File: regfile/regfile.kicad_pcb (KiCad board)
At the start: 2 copper layers, 5 parts, among them J1 Conn_01x39_Pin, U1 74LS170, U18 74LS170, U2 74LS170, U3 74LS170

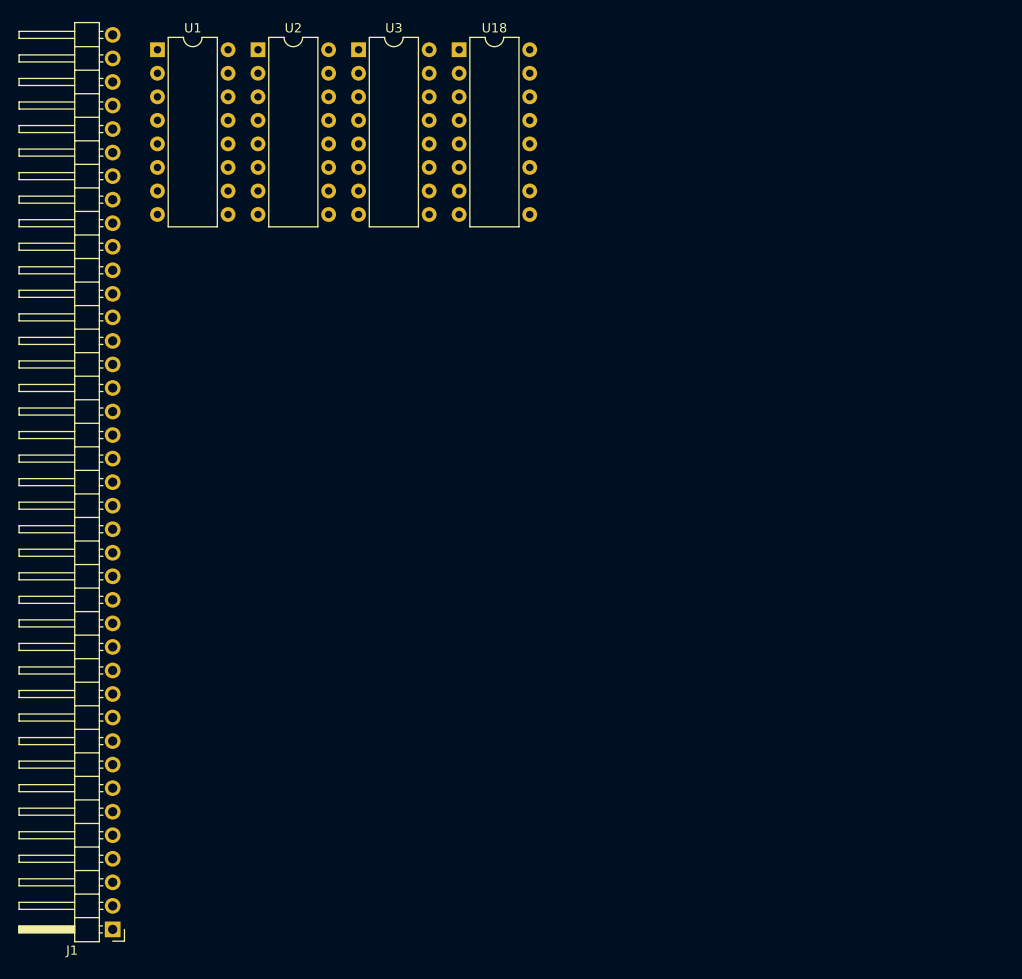
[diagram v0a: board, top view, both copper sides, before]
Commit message: fix logic for the regfile
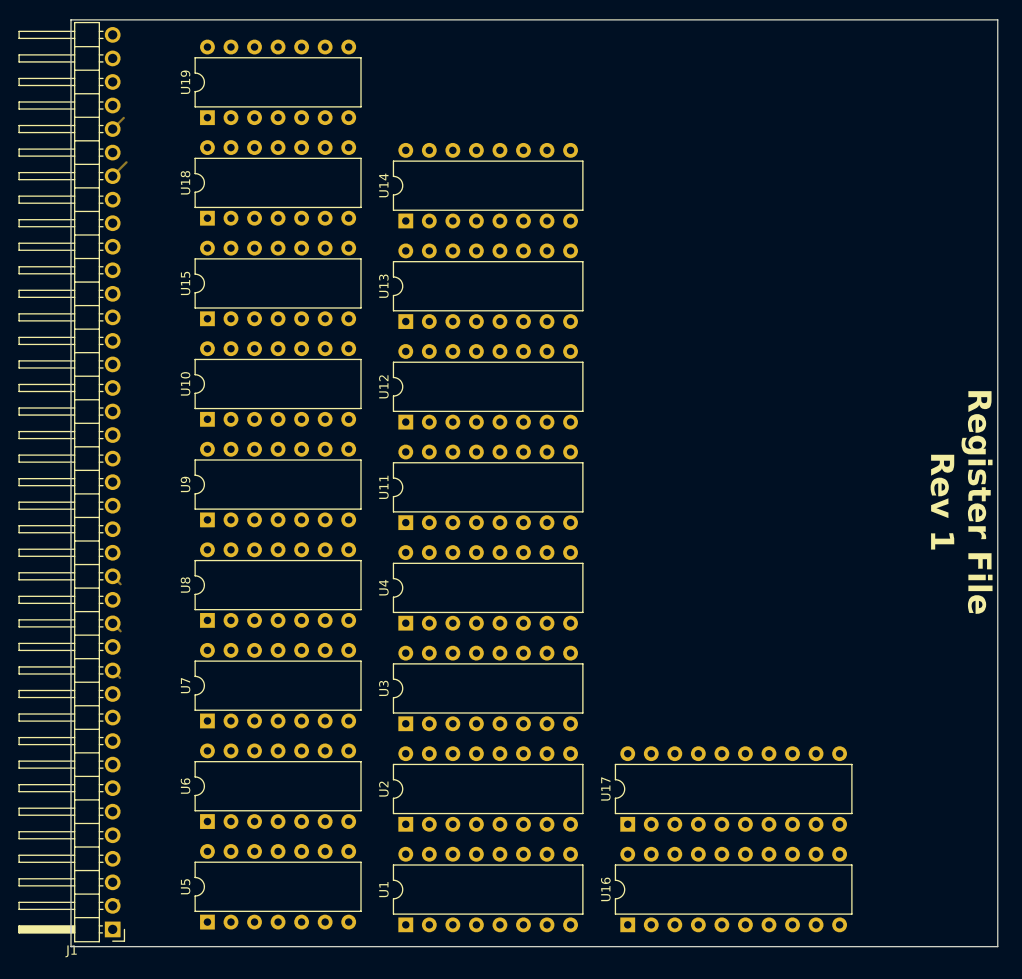
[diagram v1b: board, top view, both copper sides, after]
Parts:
- added U10: 74LS32, Package_DIP:DIP-14_W7.62mm, F.Cu at (108.2, 79.1)
- added U11: 74LS670, Package_DIP:DIP-16_W7.62mm, F.Cu at (129.6, 90.2)
- added U12: 74LS670, Package_DIP:DIP-16_W7.62mm, F.Cu at (129.6, 79.4)
- added U13: 74LS670, Package_DIP:DIP-16_W7.62mm, F.Cu at (129.6, 68.5)
- added U14: 74LS670, Package_DIP:DIP-16_W7.62mm, F.Cu at (129.6, 57.7)
- added U15: 74LS32, Package_DIP:DIP-14_W7.62mm, F.Cu at (108.2, 68.2)
- added U16: 74LS244, Package_DIP:DIP-20_W7.62mm, F.Cu at (153.6, 133.7)
- added U17: 74LS244, Package_DIP:DIP-20_W7.62mm, F.Cu at (153.6, 122.8)
- added U19: 74HC04, Package_DIP:DIP-14_W7.62mm, F.Cu at (108.2, 46.5)
- added U4: 74LS670, Package_DIP:DIP-16_W7.62mm, F.Cu at (129.6, 101.1)
- added U5: 74LS00, Package_DIP:DIP-14_W7.62mm, F.Cu at (108.2, 133.3)
- added U6: 74LS00, Package_DIP:DIP-14_W7.62mm, F.Cu at (108.2, 122.5)
- added U7: 74LS00, Package_DIP:DIP-14_W7.62mm, F.Cu at (108.2, 111.7)
- added U8: 74LS00, Package_DIP:DIP-14_W7.62mm, F.Cu at (108.2, 100.8)
- added U9: 74HC04, Package_DIP:DIP-14_W7.62mm, F.Cu at (108.2, 90.0)
- U1, U2, U3: value 74LS170 -> 74LS670
- U18: value 74LS170 -> 74LS27; footprint Package_DIP:DIP-16_W7.62mm -> Package_DIP:DIP-14_W7.62mm
- moved U1 98.2 mm to (129.6, 133.7), turned to 90 degrees
- moved U2 85.1 mm to (129.6, 122.8), turned to 90 degrees
- moved U3 72.9 mm to (129.6, 112.0), turned to 90 degrees
- moved U18 32.7 mm to (108.2, 57.4), turned to 90 degrees
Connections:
- J1 pad 10: unconnected-(J1-Pin_10-Pad10) -> Net-(J1-Pin_10)
- J1 pad 11: unconnected-(J1-Pin_11-Pad11) -> Net-(J1-Pin_11)
- J1 pad 12: unconnected-(J1-Pin_12-Pad12) -> Net-(J1-Pin_12)
- J1 pad 13: unconnected-(J1-Pin_13-Pad13) -> Net-(J1-Pin_13)
- J1 pad 14: unconnected-(J1-Pin_14-Pad14) -> Net-(J1-Pin_14)
- J1 pad 15: unconnected-(J1-Pin_15-Pad15) -> Net-(J1-Pin_15)
- J1 pad 16: unconnected-(J1-Pin_16-Pad16) -> Net-(J1-Pin_16)
- J1 pad 17: unconnected-(J1-Pin_17-Pad17) -> Net-(J1-Pin_17)
- J1 pad 18: unconnected-(J1-Pin_18-Pad18) -> Net-(J1-Pin_18)
- J1 pad 19: unconnected-(J1-Pin_19-Pad19) -> Net-(J1-Pin_19)
- J1 pad 20: unconnected-(J1-Pin_20-Pad20) -> Net-(J1-Pin_20)
- J1 pad 21: unconnected-(J1-Pin_21-Pad21) -> Net-(J1-Pin_21)
- J1 pad 22: unconnected-(J1-Pin_22-Pad22) -> Net-(J1-Pin_22)
- J1 pad 23: unconnected-(J1-Pin_23-Pad23) -> Net-(J1-Pin_23)
- J1 pad 24: unconnected-(J1-Pin_24-Pad24) -> Net-(J1-Pin_24)
- J1 pad 25: unconnected-(J1-Pin_25-Pad25) -> Net-(J1-Pin_25)
- J1 pad 26: unconnected-(J1-Pin_26-Pad26) -> Net-(J1-Pin_26)
- J1 pad 27: unconnected-(J1-Pin_27-Pad27) -> Net-(J1-Pin_27)
- J1 pad 28: unconnected-(J1-Pin_28-Pad28) -> Net-(J1-Pin_28)
- J1 pad 29: unconnected-(J1-Pin_29-Pad29) -> Net-(J1-Pin_29)
- J1 pad 30: unconnected-(J1-Pin_30-Pad30) -> Net-(J1-Pin_30)
- J1 pad 31: unconnected-(J1-Pin_31-Pad31) -> Net-(J1-Pin_31)
- J1 pad 32: unconnected-(J1-Pin_32-Pad32) -> Net-(J1-Pin_32)
- J1 pad 33: unconnected-(J1-Pin_33-Pad33) -> Net-(J1-Pin_33)
- J1 pad 34: unconnected-(J1-Pin_34-Pad34) -> Net-(J1-Pin_34)
- J1 pad 35: unconnected-(J1-Pin_35-Pad35) -> Net-(J1-Pin_35)
- J1 pad 36: unconnected-(J1-Pin_36-Pad36) -> Net-(J1-Pin_36)
- J1 pad 37: unconnected-(J1-Pin_37-Pad37) -> Net-(J1-Pin_37)
- J1 pad 38: unconnected-(J1-Pin_38-Pad38) -> Net-(J1-Pin_38)
- J1 pad 39: unconnected-(J1-Pin_39-Pad39) -> Net-(J1-Pin_39)
- J1 pad 7: unconnected-(J1-Pin_7-Pad7) -> Net-(J1-Pin_7)
- J1 pad 8: unconnected-(J1-Pin_8-Pad8) -> Net-(J1-Pin_8)
- J1 pad 9: unconnected-(J1-Pin_9-Pad9) -> Net-(J1-Pin_9)
- U1 pad 1: unconnected-(U1-D2-Pad1) -> Net-(J1-Pin_17)
- U1 pad 10: unconnected-(U1-Q1-Pad10) -> Net-(J1-Pin_24)
- U1 pad 11: unconnected-(U1-~{Er}-Pad11) -> Net-(U1-~{Er})
- U1 pad 12: unconnected-(U1-~{Ew}-Pad12) -> Net-(U1-~{Ew})
- U1 pad 13: unconnected-(U1-Wb-Pad13) -> Net-(J1-Pin_8)
- U1 pad 14: unconnected-(U1-Wa-Pad14) -> Net-(J1-Pin_7)
- U1 pad 15: unconnected-(U1-D1-Pad15) -> Net-(J1-Pin_16)
- U1 pad 2: unconnected-(U1-D3-Pad2) -> Net-(J1-Pin_18)
- U1 pad 3: unconnected-(U1-D4-Pad3) -> Net-(J1-Pin_19)
- U1 pad 4: unconnected-(U1-Rb-Pad4) -> Net-(J1-Pin_11)
- U1 pad 5: unconnected-(U1-Ra-Pad5) -> Net-(J1-Pin_10)
- U1 pad 6: unconnected-(U1-Q4-Pad6) -> Net-(J1-Pin_27)
- U1 pad 7: unconnected-(U1-Q3-Pad7) -> Net-(J1-Pin_26)
- U1 pad 9: unconnected-(U1-Q2-Pad9) -> Net-(J1-Pin_25)
- U18 pad 1: unconnected-(U18-D2-Pad1) -> Net-(J1-Pin_10)
- U18 pad 10: unconnected-(U18-Q1-Pad10) -> GND
- U18 pad 11: unconnected-(U18-~{Er}-Pad11) -> GND
- U18 pad 12: unconnected-(U18-~{Ew}-Pad12) -> ZR_addr1
- U18 pad 13: unconnected-(U18-Wb-Pad13) -> Net-(J1-Pin_12)
- U18 pad 14: unconnected-(U18-Wa-Pad14) -> +5V
- U18 pad 2: unconnected-(U18-D3-Pad2) -> Net-(J1-Pin_11)
- U18 pad 3: unconnected-(U18-D4-Pad3) -> Net-(J1-Pin_15)
- U18 pad 4: unconnected-(U18-Rb-Pad4) -> Net-(J1-Pin_14)
- U18 pad 5: unconnected-(U18-Ra-Pad5) -> Net-(J1-Pin_13)
- U18 pad 6: unconnected-(U18-Q4-Pad6) -> ZR_addr2
- U18 pad 7: unconnected-(U18-Q3-Pad7) -> GND
- U18 pad 8: GND -> unconnected-(U18-Pad8)
- U18 pad 9: unconnected-(U18-Q2-Pad9) -> GND
- U2 pad 1: unconnected-(U2-D2-Pad1) -> Net-(J1-Pin_21)
- U2 pad 10: unconnected-(U2-Q1-Pad10) -> Net-(J1-Pin_28)
- U2 pad 11: unconnected-(U2-~{Er}-Pad11) -> Net-(U2-~{Er})
- U2 pad 12: unconnected-(U2-~{Ew}-Pad12) -> Net-(U2-~{Ew})
- U2 pad 13: unconnected-(U2-Wb-Pad13) -> Net-(J1-Pin_8)
- U2 pad 14: unconnected-(U2-Wa-Pad14) -> Net-(J1-Pin_7)
- U2 pad 15: unconnected-(U2-D1-Pad15) -> Net-(J1-Pin_20)
- U2 pad 2: unconnected-(U2-D3-Pad2) -> Net-(J1-Pin_22)
- U2 pad 3: unconnected-(U2-D4-Pad3) -> Net-(J1-Pin_23)
- U2 pad 4: unconnected-(U2-Rb-Pad4) -> Net-(J1-Pin_11)
- U2 pad 5: unconnected-(U2-Ra-Pad5) -> Net-(J1-Pin_10)
- U2 pad 6: unconnected-(U2-Q4-Pad6) -> Net-(J1-Pin_31)
- U2 pad 7: unconnected-(U2-Q3-Pad7) -> Net-(J1-Pin_30)
- U2 pad 9: unconnected-(U2-Q2-Pad9) -> Net-(J1-Pin_29)
- U3 pad 1: unconnected-(U3-D2-Pad1) -> Net-(J1-Pin_17)
- U3 pad 10: unconnected-(U3-Q1-Pad10) -> Net-(J1-Pin_24)
- U3 pad 11: unconnected-(U3-~{Er}-Pad11) -> Net-(U3-~{Er})
- U3 pad 12: unconnected-(U3-~{Ew}-Pad12) -> Net-(U3-~{Ew})
- U3 pad 13: unconnected-(U3-Wb-Pad13) -> Net-(J1-Pin_8)
- U3 pad 14: unconnected-(U3-Wa-Pad14) -> Net-(J1-Pin_7)
- U3 pad 15: unconnected-(U3-D1-Pad15) -> Net-(J1-Pin_16)
- U3 pad 2: unconnected-(U3-D3-Pad2) -> Net-(J1-Pin_18)
- U3 pad 3: unconnected-(U3-D4-Pad3) -> Net-(J1-Pin_19)
- U3 pad 4: unconnected-(U3-Rb-Pad4) -> Net-(J1-Pin_11)
- U3 pad 5: unconnected-(U3-Ra-Pad5) -> Net-(J1-Pin_10)
- U3 pad 6: unconnected-(U3-Q4-Pad6) -> Net-(J1-Pin_27)
- U3 pad 7: unconnected-(U3-Q3-Pad7) -> Net-(J1-Pin_26)
- U3 pad 9: unconnected-(U3-Q2-Pad9) -> Net-(J1-Pin_25)
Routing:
- net Net-(J1-Pin_33): track 0.00 -> 2.11 mm
- net Net-(J1-Pin_35): track 0.00 -> 1.70 mm
- net Net-(J1-Pin_16): track 0.00 -> 1.20 mm
- net Net-(J1-Pin_14): track 0.00 -> 1.20 mm
- net Net-(J1-Pin_12): track 0.00 -> 1.13 mm
- net +5V: track 0.00 -> 0.85 mm
- net Net-(J1-Pin_28): track 0.00 -> 0.79 mm
- net Net-(J1-Pin_29): track 0.00 -> 0.74 mm
- net read enable 1: track 0.00 -> 0.74 mm
- net write enable: track 0.00 -> 0.58 mm
- net Net-(J1-Pin_7): track 0.00 -> 0.57 mm
- net Net-(J1-Pin_8): track 0.00 -> 0.51 mm
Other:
- board outline added: 100 x 100 mm
- board text added: "Register File Rev 1"

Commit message: finish regfile
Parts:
- removed U10, U15: 74LS32, Package_DIP:DIP-14_W7.62mm
- removed U19, U9: 74HC04, Package_DIP:DIP-14_W7.62mm
- U5, U7: value 74LS00 -> 74HC00
- U6: value 74LS00 -> 74HC04
- U8: value 74LS00 -> 74LS32
- moved U1 95.0 mm to (112.7, 40.1), turned to 0 degrees
- moved U8 73.0 mm to (171.2, 63.9), turned to 0 degrees
- moved U7 68.1 mm to (171.0, 85.3), turned to 0 degrees
- moved U6 62.0 mm to (131.2, 64.9), turned to 0 degrees
- moved U2 61.0 mm to (112.7, 64.2), turned to 0 degrees
- moved U14 58.3 mm to (150.5, 112.1), turned to 0 degrees
- moved U11 54.3 mm to (150.5, 40.1), turned to 0 degrees
- moved U5 52.7 mm to (131.2, 85.9), turned to 0 degrees
- moved U16 31.8 mm to (171.0, 107.0), turned to 0 degrees
- moved U3 29.0 mm to (112.7, 88.4), turned to 0 degrees
- moved U13 28.6 mm to (150.5, 88.1), turned to 0 degrees
- moved U17 27.3 mm to (131.0, 107.4), turned to 0 degrees
- moved U18 26.6 mm to (130.9, 43.5), turned to 0 degrees
- moved U12 25.9 mm to (150.5, 64.1), turned to 0 degrees
- moved U4 20.4 mm to (112.7, 112.4), turned to 0 degrees
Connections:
- U1 pad 11: Net-(U1-~{Er}) -> read enable L bank 1
- U1 pad 12: Net-(U1-~{Ew}) -> write enable bank 1
- U11 pad 11: Net-(U11-~{Er}) -> read enable R bank 1
- U11 pad 12: Net-(U11-~{Ew}) -> write enable bank 1
- U12 pad 11: Net-(U12-~{Er}) -> read enable R bank 1
- U12 pad 12: Net-(U12-~{Ew}) -> write enable bank 1
- U13 pad 11: Net-(U13-~{Er}) -> read enable R bank 2
- U13 pad 12: Net-(U13-~{Ew}) -> write enable bank 2
- U14 pad 11: Net-(U14-~{Er}) -> read enable R bank 2
- U14 pad 12: Net-(U14-~{Ew}) -> write enable bank 2
- U2 pad 11: Net-(U2-~{Er}) -> read enable L bank 1
- U2 pad 12: Net-(U2-~{Ew}) -> write enable bank 1
- U3 pad 11: Net-(U3-~{Er}) -> read enable L bank 2
- U3 pad 12: Net-(U3-~{Ew}) -> write enable bank 2
- U4 pad 11: Net-(U4-~{Er}) -> read enable L bank 2
- U4 pad 12: Net-(U4-~{Ew}) -> write enable bank 2
- U5 pad 10: Net-(U5-Pad10) -> Net-(J1-Pin_12)
- U5 pad 11: Net-(U10-Pad4) -> Net-(U5-Pad11)
- U5 pad 13: unconnected-(U5-Pad13) -> Net-(U5-Pad13)
- U5 pad 2: Net-(U5-Pad2) -> Net-(J1-Pin_9)
- U5 pad 3: Net-(U1-~{Ew}) -> write enable bank 1
- U5 pad 4: read enable 1 -> write enable
- U5 pad 6: Net-(U10-Pad1) -> write enable bank 2
- U5 pad 8: Net-(U2-~{Ew}) -> Net-(U5-Pad8)
- U5 pad 9: write enable -> read enable 1
- U6 pad 1: write enable -> Net-(J1-Pin_9)
- U6 pad 10: Net-(J1-Pin_9) -> unconnected-(U6-Pad10)
- U6 pad 11: Net-(U10-Pad12) -> GND
- U6 pad 12: read enable 1 -> unconnected-(U6-Pad12)
- U6 pad 13: Net-(J1-Pin_12) -> GND
- U6 pad 2: Net-(J1-Pin_9) -> Net-(U5-Pad5)
- U6 pad 3: Net-(U3-~{Ew}) -> Net-(J1-Pin_12)
- U6 pad 4: read enable 1 -> Net-(U5-Pad13)
- U6 pad 5: Net-(J1-Pin_12) -> Net-(J1-Pin_15)
- U6 pad 6: Net-(U10-Pad9) -> Net-(U6-Pad6)
- U6 pad 8: Net-(U4-~{Ew}) -> unconnected-(U6-Pad8)
- U6 pad 9: write enable -> GND
- U7 pad 1: write enable -> read enable 2
- U7 pad 10: Net-(U19-Pad2) -> GND
- U7 pad 11: Net-(U15-Pad4) -> unconnected-(U7-Pad11)
- U7 pad 12: read enable 2 -> GND
- U7 pad 13: Net-(U19-Pad4) -> GND
- U7 pad 2: Net-(U7-Pad2) -> Net-(U6-Pad6)
- U7 pad 3: Net-(U11-~{Ew}) -> Net-(U7-Pad3)
- U7 pad 5: Net-(U7-Pad5) -> Net-(J1-Pin_15)
- U7 pad 6: Net-(U15-Pad1) -> Net-(U7-Pad6)
- U7 pad 8: Net-(U12-~{Ew}) -> unconnected-(U7-Pad8)
- U7 pad 9: write enable -> GND
- U8 pad 1: write enable -> Net-(U5-Pad8)
- U8 pad 10: Net-(J1-Pin_9) -> ZR_addr2
- U8 pad 11: Net-(U15-Pad12) -> read enable R bank 2
- U8 pad 12: read enable 2 -> Net-(U7-Pad3)
- U8 pad 13: Net-(J1-Pin_15) -> ZR_addr2
- U8 pad 2: Net-(J1-Pin_9) -> ZR_addr1
- U8 pad 3: Net-(U13-~{Ew}) -> read enable L bank 1
- U8 pad 4: read enable 2 -> Net-(U5-Pad11)
- U8 pad 5: Net-(J1-Pin_15) -> ZR_addr1
- U8 pad 6: Net-(U15-Pad9) -> read enable L bank 2
- U8 pad 8: Net-(U14-~{Ew}) -> read enable R bank 1
- U8 pad 9: write enable -> Net-(U7-Pad6)
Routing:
- net GND: track 0.00 -> 523.0 mm, vias 0 -> 17
- net +5V: track 0.85 -> 439.3 mm, vias 0 -> 4
- net Net-(J1-Pin_8): track 0.51 -> 220.4 mm, vias 0 -> 9
- net Net-(J1-Pin_7): track 0.57 -> 217.8 mm, vias 0 -> 3
- net Net-(J1-Pin_39): track 0.00 -> 194.6 mm, vias 0 -> 8
- net Net-(J1-Pin_38): track 0.00 -> 191.2 mm, vias 0 -> 5
- net Net-(J1-Pin_37): track 0.00 -> 185.4 mm, vias 0 -> 12
- net Net-(J1-Pin_34): track 0.00 -> 184.4 mm, vias 0 -> 8
- net Net-(J1-Pin_19): track 0.00 -> 176.6 mm, vias 0 -> 7
- net Net-(J1-Pin_13): track 0.00 -> 170.9 mm, vias 0 -> 7
- net Net-(J1-Pin_23): track 0.00 -> 169.5 mm, vias 0 -> 7
- net Net-(J1-Pin_35): track 1.70 -> 170.4 mm, vias 0 -> 9
- net Net-(J1-Pin_22): track 0.00 -> 168.2 mm, vias 0 -> 11
- net Net-(J1-Pin_36): track 0.00 -> 167.4 mm, vias 0 -> 10
- net Net-(J1-Pin_14): track 1.20 -> 167.1 mm, vias 0 -> 7
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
